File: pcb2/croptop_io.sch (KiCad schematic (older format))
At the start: 77 parts

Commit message: Added USB port control
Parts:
- removed C? (x3): 0.1uF, Capacitor_SMD:C_0402_1005Metric, symbol Device:C_Small
- removed R? (x6): 100, Resistor_SMD:R_0402_1005Metric, symbol Device:R
- removed R? (x3): 2K, Resistor_SMD:R_0402_1005Metric, symbol Device:R
- removed R? (x4): R, symbol Device:R
- removed R? (x4): 22, Resistor_SMD:R_0402_1005Metric, symbol Device:R
- removed R? (x2): 10, Resistor_SMD:R_0402_1005Metric, symbol Device:R
- removed TP? (x5): TestPoint, symbol Connector:TestPoint
- removed U? (x2): DT6250-06MR-13, Package_SO:MSOP-8_3x3mm_P0.65mm, symbol CropTop:DT6250-06MR-13
- added C? (x3): 0.1uF, Capacitor_SMD:C_0402_1005Metric, symbol Device:C
- added J?: Load Cell Block, symbol Connector:Screw_Terminal_01x16
- added J?: Motor Drive Block, symbol Connector:Screw_Terminal_01x08
- added R? (x3): 2kΩ, symbol Device:R
- added R? (x6): 22Ω, symbol Device:R
- added R? (x4): Ω, symbol Device:R
- added R? (x6): 100Ω, symbol Device:R
- added TP? (x5): TestPoint, symbol Connector:TestPoint
- added U? (x2): TPD4E1U06, symbol CropTop:TPD4E1U06
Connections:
- net labels added: +BATT, ADC_CS, ADC_MISO, ADC_MOSI, ADC_SCLK, DC_FAULT, DC_OUT1, DC_OUT2, DC_PWM_1, DC_PWM_2
- net labels removed: AUX_BATTERY, CS_1, DRV_FLT, DRV_IN1, DRV_IN2, DRV_OUT1, DRV_OUT2, MISO_1, MOSI_1, SCLK_1
- wire segments 345 -> 417
- no-connect marks 10 -> 14
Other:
- note added: "24-bit ΔΣ ADC Load Cell Interface"
- note removed: "Force Sensor Interface w/ ADC and Buffer"
- moved on the sheet: C?, D?, J?, L?, Q?, R?, TP?, U?

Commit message: Schematic near completion
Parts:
- added C?: 0.1uF, Capacitor_SMD:C_0402_1005Metric, symbol Device:C
- added U? (x2): TPD4E1U06, symbol CropTop:TPD4E1U06
- C? (x5): footprint Capacitor_SMD:C_0805_2012Metric -> Capacitor_SMD:C_0402_1005Metric
- J?: Note (none) -> Rotary Encoder
- J?: Note (none) -> Load Cell
- J?: Note (none) -> Motor Drive Block
- R? (x3): value 2kΩ -> 10k; footprint (none) -> Resistor_SMD:R_0402_1005Metric
- R? (x6): value 22Ω -> 22; footprint (none) -> Resistor_SMD:R_0402_1005Metric
- R? (x4): footprint (none) -> Resistor_SMD:R_0402_1005Metric
- R? (x6): value 100Ω -> 100; footprint (none) -> Resistor_SMD:R_0402_1005Metric
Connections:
- wire segments 417 -> 433
- no-connect marks 14 -> 18
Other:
- note added: "D.N.P."
- note added: "DC Motor & Stepper Motor Driver Interface"
- note added: "Low Noise 5V Plane"
- note removed: "DC Motor & Stepper Motor Drivers"
- note removed: "Isolated 5V Plane"
- moved on the sheet: C?, J?, L?, R?, TP?, U?

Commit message: Added pmod
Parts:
- removed C?: 10uF, Capacitor_SMD:C_0402_1005Metric, symbol Device:C
- removed C?: 0.1uF, Capacitor_SMD:C_0402_1005Metric, symbol Device:C
- removed J?: Rotary Encoder Term. Block, symbol Connector:Screw_Terminal_01x08
- removed J?: Load Cell Block, symbol Connector:Screw_Terminal_01x16
- removed L?: 10uH, Inductor_SMD:L_1210_3225Metric, symbol Device:L
- removed R? (x3): 0, Resistor_SMD:R_0402_1005Metric, symbol Device:R
- removed U?: PUSBM5V5X4, croptop:PUSBM5V5X4, symbol CropTop:PUSBM5V5X4
- removed U?: 74HCT125D, Package_SO:SOIC-14_3.9x8.7mm_P1.27mm, symbol CropTop:74LVC125A
- removed U? (x2): TPD4E1U06, symbol CropTop:TPD4E1U06
- added C? (x7): 10uF, Capacitor_SMD:C_0402_1005Metric, symbol Device:C
- added C?: 0.1uF, Capacitor_SMD:C_0402_1005Metric, symbol Device:C
- added D? (x3): LTSTC171GKT, LED_SMD:LED_0805_2012Metric, symbol Device:LED
- added J?: 39357-0015, symbol Connector:Screw_Terminal_01x15
- added J?: 39357-0006, symbol Connector:Screw_Terminal_01x06
- added J?: 39357-0006, symbol Connector:Screw_Terminal_01x04
- added JP?: N.0., symbol Jumper:SolderJumper_2_Open
- added L?: BKP1005HS121, symbol Device:L_Core_Ferrite
- added R? (x2): 100, Resistor_SMD:R_0402_1005Metric, symbol Device:R
- added R? (x6): 10k, Resistor_SMD:R_0402_1005Metric, symbol Device:R
- added R? (x3): 220, Resistor_SMD:R_0402_1005Metric, symbol Device:R
- added TP? (x13): TestPoint, symbol Connector:TestPoint
- added U? (x3): AP22802AW5, symbol CropTop:AP22802AW5
- added U? (x2): TPD4E1U06, symbol CropTop:TPD4E1U06
- D?: value D_Schottky -> NSR0240HT1G
- J?: value Motor Drive Block -> 39357-0008
- Q?: value Q_PMOS_DGS -> FDMA530PZ
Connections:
- net labels added: ADI_5V_FLG, DC_OUT_1, DC_OUT_2, LINCODE_1, LINCODE_2, LINCODE_PWR_FLG, ROTARY_1A, ROTARY_1B, ROTARY_2A, ROTARY_2B, ROTARY_PWR_FLG, ~ADC_CS, ~DC_FAULT
- net labels removed: +BATT, ADC_CS, DC_FAULT, DC_OUT1, DC_OUT2, INPUT_CAP_1, INPUT_CAP_2, INPUT_CAP_3, INPUT_CAP_4, LIN_GND, LIN_IN, LIN_VOLT, ROT_A1, ROT_A2, ROT_GND, ROT_VDD, ROT_Y1, ROT_Y2
- wire segments 433 -> 525
- no-connect marks 18 -> 8
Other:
- note removed: "Check pinout of PMOS"
- note removed: "D.N.P."
- note removed: "DNP one"
- moved on the sheet: C?, D?, J?, Q?, R?, TP?, U?

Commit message: pwm
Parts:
- removed C?: 0.1uF, Capacitor_SMD:C_0402_1005Metric, symbol Device:C
- removed J?: 39357-0006, symbol Connector:Screw_Terminal_01x06
- removed J?: 39357-0006, symbol Connector:Screw_Terminal_01x04
- removed R? (x2): Ω, Resistor_SMD:R_0402_1005Metric, symbol Device:R
- removed TP? (x10): TestPoint, symbol Connector:TestPoint
- removed U?: A5984, symbol CropTop:A5984
- removed U?: TPD4E1U06, symbol CropTop:TPD4E1U06
- added C55, C61, C?: 0.1uF, Capacitor_SMD:C_0402_1005Metric, symbol Device:C
- added C68, C70: 10uF, Capacitor_SMD:C_0402_1005Metric, symbol Device:C
- added J10: 39357-0008, symbol Connector:Screw_Terminal_01x08
- added R74, R75, R77, R78: 110mΩ, symbol Device:R
- added R76: 1MΩ, symbol Device:R
- added R86, R87: 22Ω, Resistor_SMD:R_0402_1005Metric, symbol Device:R
- added TP109, TP111, TP68, TP69, TP70, TP72, TP73, TP76, TP77, TP78, TP79, TP80, TP81, TP85, TP86, TP87, TP88, TP91, TP95, TP96, TP97: TestPoint, symbol Connector:TestPoint
- added U14: DRV8825, symbol CropTop:DRV8825
- R64, R65, R70, R88, R89, R91, R93, R94, R95: renamed from R?; value 10k -> 10kΩ
- R66, R67, R68, R69, R71, R72: renamed from R?; value 22 -> 22Ω
- R73: renamed from R?; value Ω -> 110mΩ; footprint Resistor_SMD:R_0402_1005Metric -> (none)
- R79: renamed from R?; value Ω -> 10kΩ
- R80, R81, R82, R83, R84, R85, R92, R96: renamed from R?; value 100 -> 100Ω
- R90: renamed from R?; value 0 -> 0Ω
- R97, R98, R99: renamed from R?; value 220 -> 220Ω
- gave numbers to parts that had none: 69
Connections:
- net labels added: STEP_DECAY, STEP_MODE0, STEP_MODE1, STEP_MODE2, ~STEP_ENBL, ~STEP_FAULT, ~STEP_HOME
- net labels removed: DC_OUT_1, DC_OUT_2, ROTARY_2A, ROTARY_2B, STEP_FAULT, STEP_MS1, STEP_MS2, STEP_MS3, STEP_OUT1A, STEP_OUT1B, STEP_OUT2A, STEP_OUT2B, ~STEP_ENABLE
- wire segments 525 -> 557
- no-connect marks 8 -> 10
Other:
- note added: "DRV8825\nMax Current: 2.5A\nCurrent Limit: 3.3/5*R"
- note added: "DRV8872\nMax Current: 3.5A\nCurrent Limit: 0.35/R"
- note added: "RL1220S-R11"
- note removed: "I think I can\njust tie this\nto 3v3?"
- note removed: "Rotary Encoder Interface"
- moved on the sheet: C51, C53, C54, C57, C63, C64, C66, C67, C72, D11, D12, D14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

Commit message: Added TVS diodes
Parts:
- removed J10: 39357-0008, symbol Connector:Screw_Terminal_01x08
- added C47, C56: 10uF, Capacitor_SMD:C_0402_1005Metric, symbol Device:C
- added D14: LTSTC171GKT, LED_SMD:LED_0805_2012Metric, symbol Device:LED
- added D15, D16, D18, D21: TPD1E6B06, symbol Device:D_TVS
- added D22, D23, D24, D25: TPD2E007, symbol Device:D_TVS_x2_AAC
- added J10, J8, J9: 39357-0004, symbol Connector:Screw_Terminal_01x04
- added R71, R72: 10kΩ, Resistor_SMD:R_0402_1005Metric, symbol Device:R
- added R75: 100Ω, Resistor_SMD:R_0402_1005Metric, symbol Device:R
- added R79, R80, R83, R84: 220Ω, Resistor_SMD:R_0402_1005Metric, symbol Device:R
- added TP67, TP69, TP76, TP77: TestPoint, symbol Connector:TestPoint
- added U23: AP22802AW5, symbol CropTop:AP22802AW5
- added U27: TPD4E1U06, symbol CropTop:TPD4E1U06
- gave numbers to parts that had none: 1
- renumbered C64 to C45, C63 to C46, C45 to C48, C46 to C49, C47 to C50, C66 to C51, C67 to C52, C48 to C53, C49 to C54, C50 to C55, C52 to C57, C68 to C58, C56 to C59, C70 to C60, C72 to C61, C58 to C62, C59 to C63, C60 to C64, C62 to C65, C65 to C66, C51 to C67, C61 to C68, C53 to C69, C54 to C70, C57 to C72, C55 to C73, C69 to C74, C71 to C75, D12 to D13, D14 to D17, D13 to D19, D11 to D20, J9 to J11, J8 to J12, R93 to R100, R76 to R101, R96 to R102, R77 to R103, R78 to R104, R79 to R105, R88 to R63, R86 to R64, R87 to R65, R89 to R66, R66 to R67, R67 to R68, R68 to R69, R69 to R70, R92 to R73, R90 to R74, R94 to R76, R95 to R77, R97 to R78, R98 to R81, R99 to R82, R80 to R85, R81 to R86, R82 to R87, R83 to R88, R84 to R89, R85 to R90, R64 to R91, R65 to R92, R70 to R93, R71 to R94, R72 to R95, R91 to R96, R73 to R97, R74 to R98, R75 to R99, TP80 to TP100, TP81 to TP101, TP105 to TP102, TP82 to TP103, TP83 to TP104, TP84 to TP105, TP108 to TP106, TP89 to TP107, TP92 to TP108, TP93 to TP109, TP90 to TP110, TP94 to TP111, TP96 to TP60, TP97 to TP61, TP64 to TP62, TP65 to TP63, TP66 to TP64, TP67 to TP65, TP104 to TP66, TP106 to TP68, TP107 to TP70, TP110 to TP71, TP85 to TP72, TP109 to TP73, TP86 to TP74, TP111 to TP75, TP87 to TP78, TP88 to TP79, TP91 to TP80, TP95 to TP81, TP68 to TP82, TP98 to TP83, TP99 to TP84, TP69 to TP85, TP70 to TP86, TP100 to TP87, TP71 to TP88, TP101 to TP89, TP72 to TP90, TP73 to TP91, TP74 to TP92, TP102 to TP93, TP75 to TP94, TP76 to TP95, TP77 to TP96, TP103 to TP97, TP78 to TP98, TP79 to TP99, U18 to U21, U17 to U22, U12 to U24, U21 to U25, U20 to U26, U15 to U28, U16 to U29, U13 to U30, U14 to U31, U19 to U32
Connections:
- net +3V3: now also C47.1, R71.1, R72.1, U23.4 (EN), U23.5 (IN)
- net DGND: now also C47.2, C56.2, D15.1 (A1), D16.1 (A1), D18.1 (A1), D21.2 (A2), D22.3 (common), D23.3 (common), D24.3 (common), D25.3 (common), J10.4 (Pin_4), J8.4 (Pin_4), J9.4 (Pin_4), R72.2, R75.2, U23.2 (GND), U27.2 (GND)
- net at C55.2, C59.2, R87.2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: now also TP74.1
- net at C55.1, C57.2, R90.2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: now also TP72.1
- net at C53.2, C65.2, R85.2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: now also TP81.1; no longer C53.1, C64.2, R88.2, U24.6 (AIN1-)
- net at C54.2, C63.2, R86.2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: now also TP79.1
- net at C54.1, C62.2, R89.2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: now also TP78.1
- net at J12.1 (Pin_1), TP105.1, U30.6 (OUT1): now also D22.2 (A2)
- net at J12.2 (Pin_2), TP104.1, U30.8 (OUT2): now also D22.1 (A1)
- net at U22.2 (A1): now also U25.6 (D1-), R79.2; no longer U25.1 (D1+)
- net at U22.5 (A2): now also U25.1 (D1+), R80.2
- net at J12.7 (Pin_7), TP111.1, U31.10 (BOUT1): now also D25.2 (A2)
- net at J12.5 (Pin_5), TP109.1, U31.5 (AOUT1): now also D24.2 (A2)
- net at J12.6 (Pin_6), TP107.1, U31.7 (AOUT2): now also D24.1 (A1)
- net at J12.8 (Pin_8), TP110.1, U31.8 (BOUT2): now also D25.1 (A1)
- net at C74.1, C75.2, D19.2 (A)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: now also D21.1 (A1)
- net at C52.1, D13.2 (A), TP68.1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: now also D15.2 (A2), J9.1 (Pin_1)
- net at R81.1: now also J9.2 (Pin_2), U27.4 (D2-); no longer U25.4 (D2-)
- net at R82.1: now also J9.3 (Pin_3), U27.3 (D2+); no longer U25.3 (D2+)
- net at C61.1, D17.2 (A), TP71.1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: now also D18.2 (A2), J8.1 (Pin_1); no longer U25.6 (D1-)
- net at J12.3 (Pin_3), Q3.1 (D): now also D23.1 (A1), D23.2 (A2)
- net at TP80.1: now also C53.1, C64.2, R88.2, U24.6 (AIN1-)
- net LINCODE_1 renamed POTEN_1
- net LINCODE_2 renamed POTEN_2
- net LINCODE_PWR_FLG renamed POTEN_PWR_FLG
- net ROTARY_PWR_FLG renamed ENCODE_PWR_FLG
- new net: J8.2 (Pin_2), R79.1
- new net: J8.3 (Pin_3), R80.1
- new net: D14.1 (K), R75.1
- new net: C56.1, D14.2 (A), D16.2 (A2), J10.1 (Pin_1), TP69.1, U23.1 (OUT)
- new net: J10.2 (Pin_2), R83.1, U27.6 (D1-)
- new net: J10.3 (Pin_3), R84.1, U27.1 (D1+)
- new net POTEN_ECHO: R84.2, TP77.1
- new net POTEN_TRIG: R83.2, TP76.1
- new net SONIC_PWR_FLG: R71.2, TP67.1, U23.3 (FLG)
- no-connect marks 10 -> 13
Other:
- note added: "Linear/Rotary Encoder Interface"
- note added: "Linear/Rotary Potentiometer Interface"
- note added: "Ultrasonic Ranging Module Interface"
- note removed: "Linear and Rotary Encoder Interface"
- moved on the sheet: C45, C46, C48, C49, C50, C51, C52, C53, C54, C55, C57, C58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

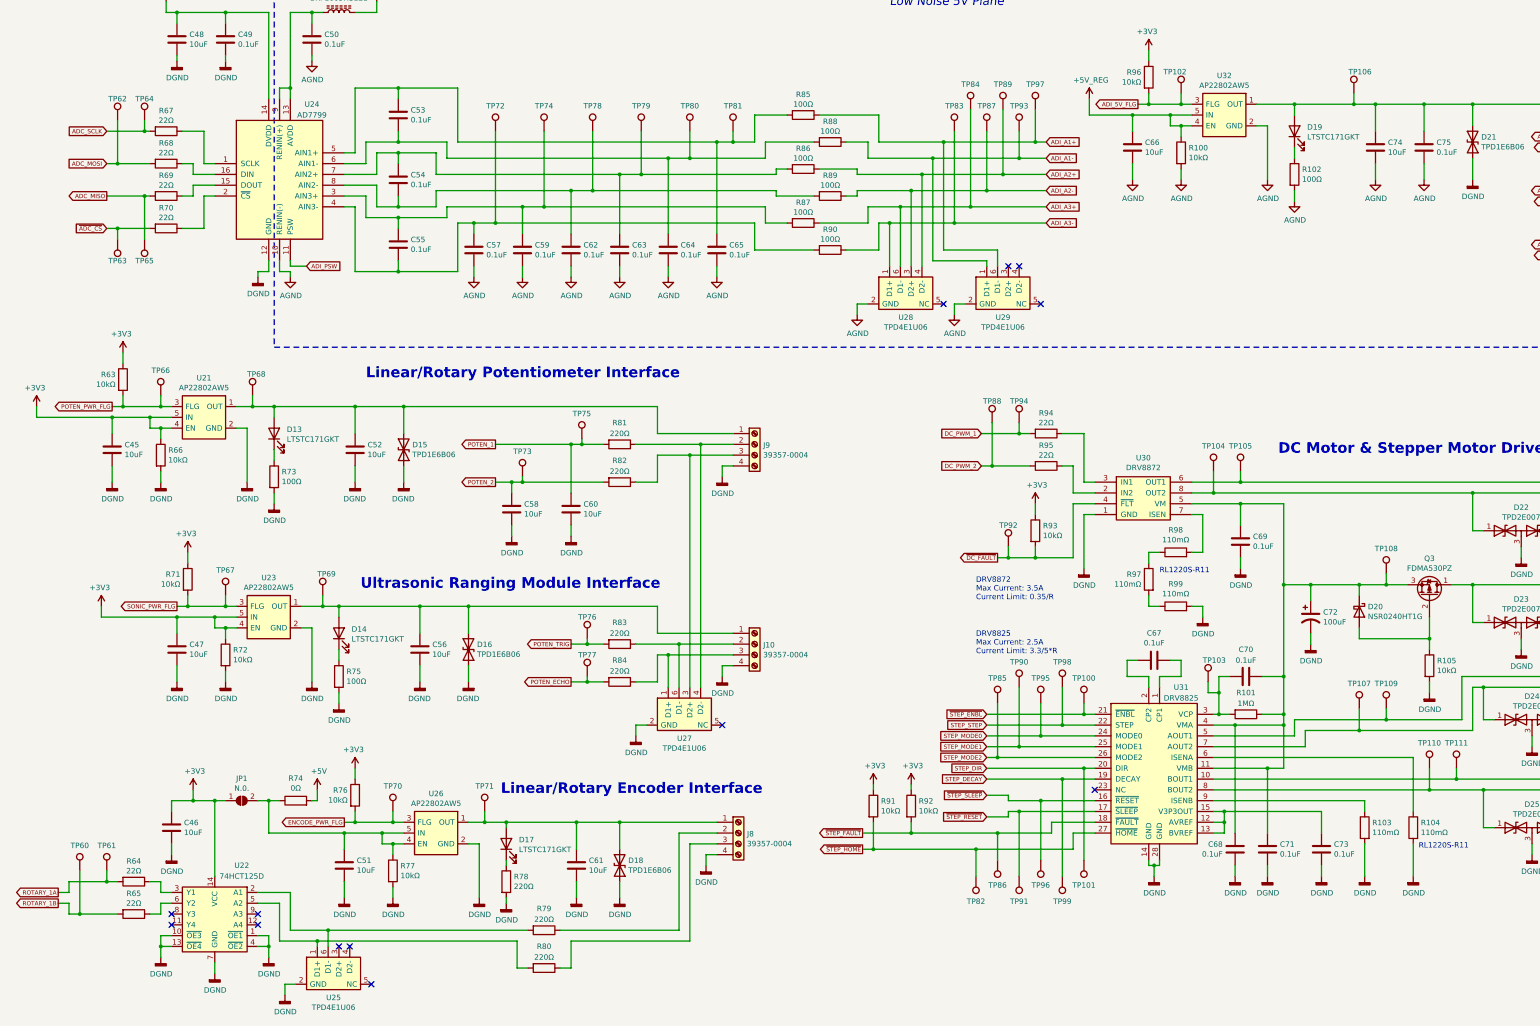
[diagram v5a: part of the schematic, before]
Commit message: Updated pin out
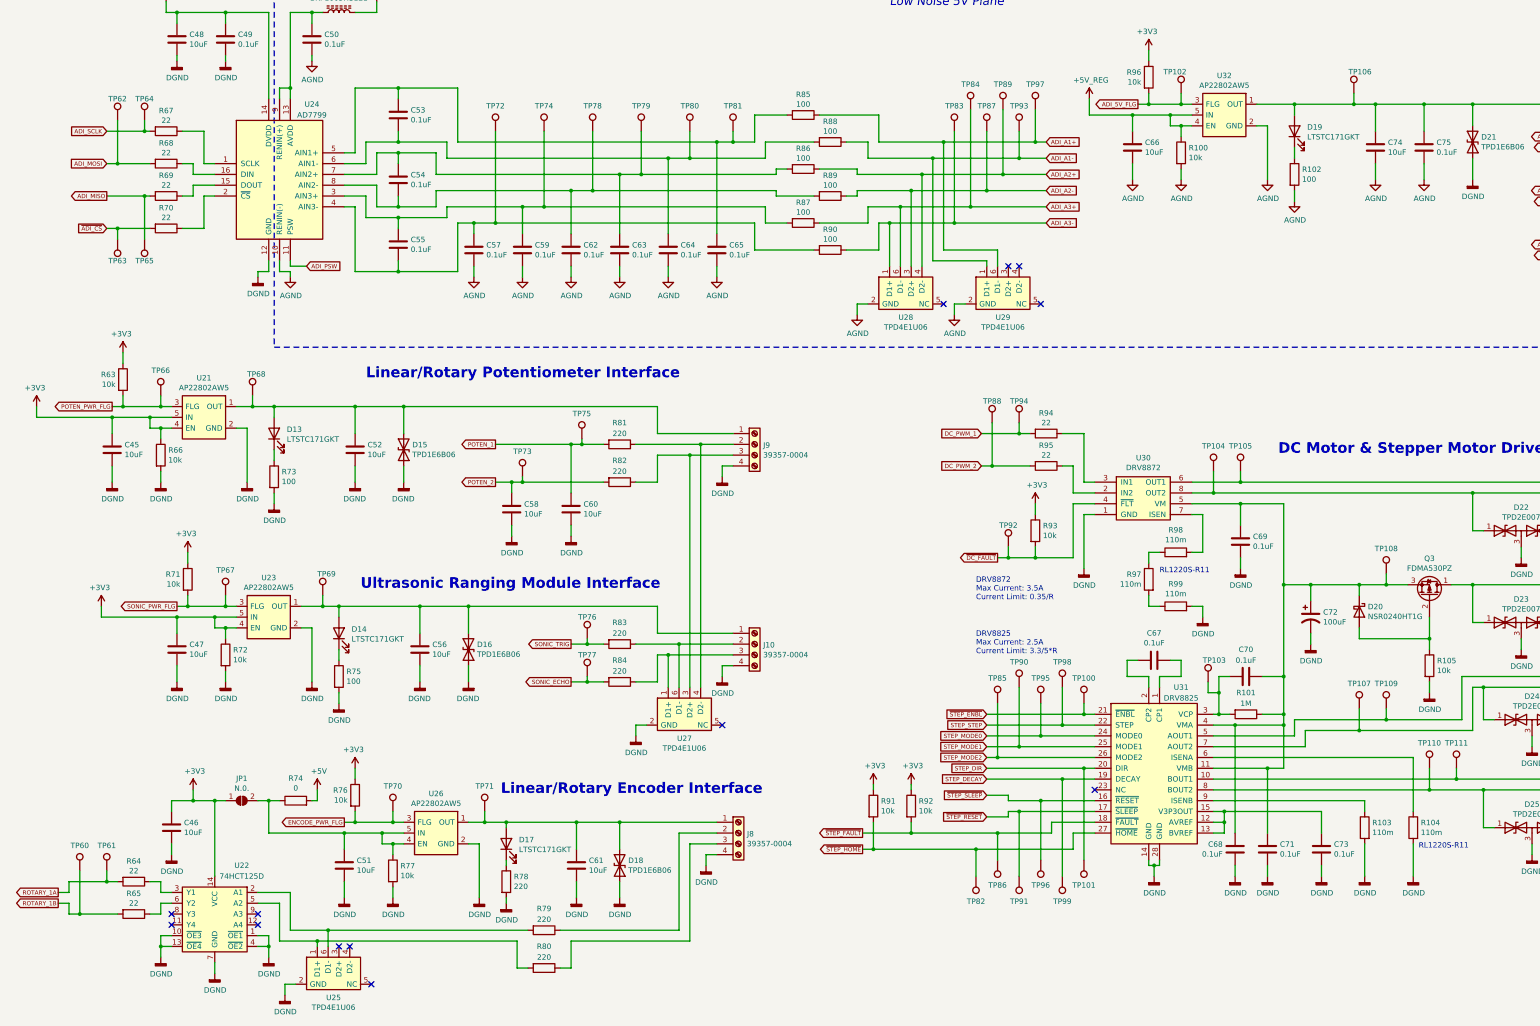
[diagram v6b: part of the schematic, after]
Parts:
- R100, R105, R63, R66, R71, R72, R76, R77, R91, R92, R93, R96: value 10kΩ -> 10k
- R101: value 1MΩ -> 1M
- R102, R73, R75, R85, R86, R87, R88, R89, R90: value 100Ω -> 100
- R103, R104, R97, R98, R99: value 110mΩ -> 110m
- R64, R65, R67, R68, R69, R70, R94, R95: value 22Ω -> 22
- R74: value 0Ω -> 0
- R78, R79, R80, R81, R82, R83, R84: value 220Ω -> 220
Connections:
- net ADC_MISO renamed ADI_MISO
- net ADC_MOSI renamed ADI_MOSI
- net ADC_SCLK renamed ADI_SCLK
- net POTEN_ECHO renamed SONIC_ECHO
- net POTEN_TRIG renamed SONIC_TRIG
- net ~ADC_CS renamed ~ADI_CS
